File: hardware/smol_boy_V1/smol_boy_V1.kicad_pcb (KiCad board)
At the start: 2 copper layers, 21 parts, among them J1 Conn_01x01_Male, J2 Conn_01x06_Male, J3 Conn_01x04_Male, J4 Conn_01x03_Male, J5 Conn_01x03_Male, J6 Conn_01x03_Male, J7 Conn_01x03_Male, J8 Conn_01x03_Male, J9 Conn_01x03_Male, U1 ESP-12E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

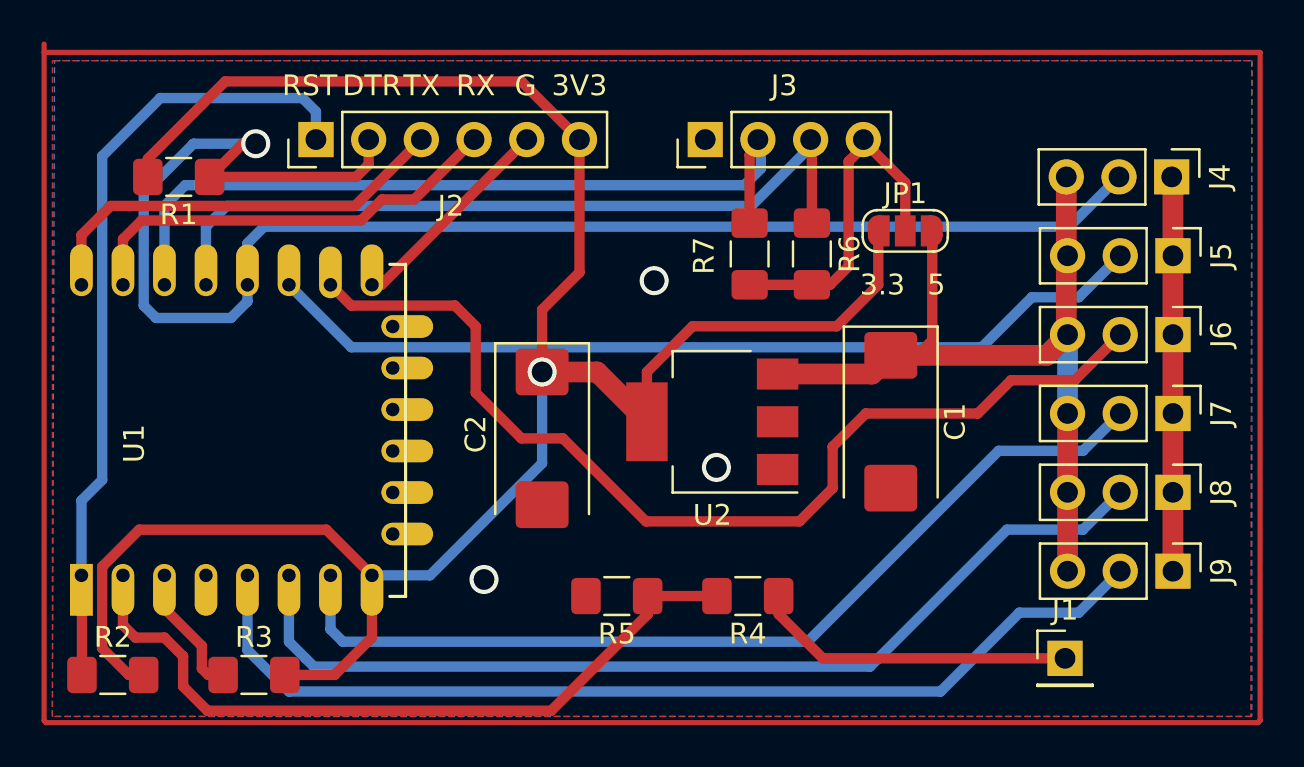
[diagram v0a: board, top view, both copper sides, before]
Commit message: fixed pcb channel pins
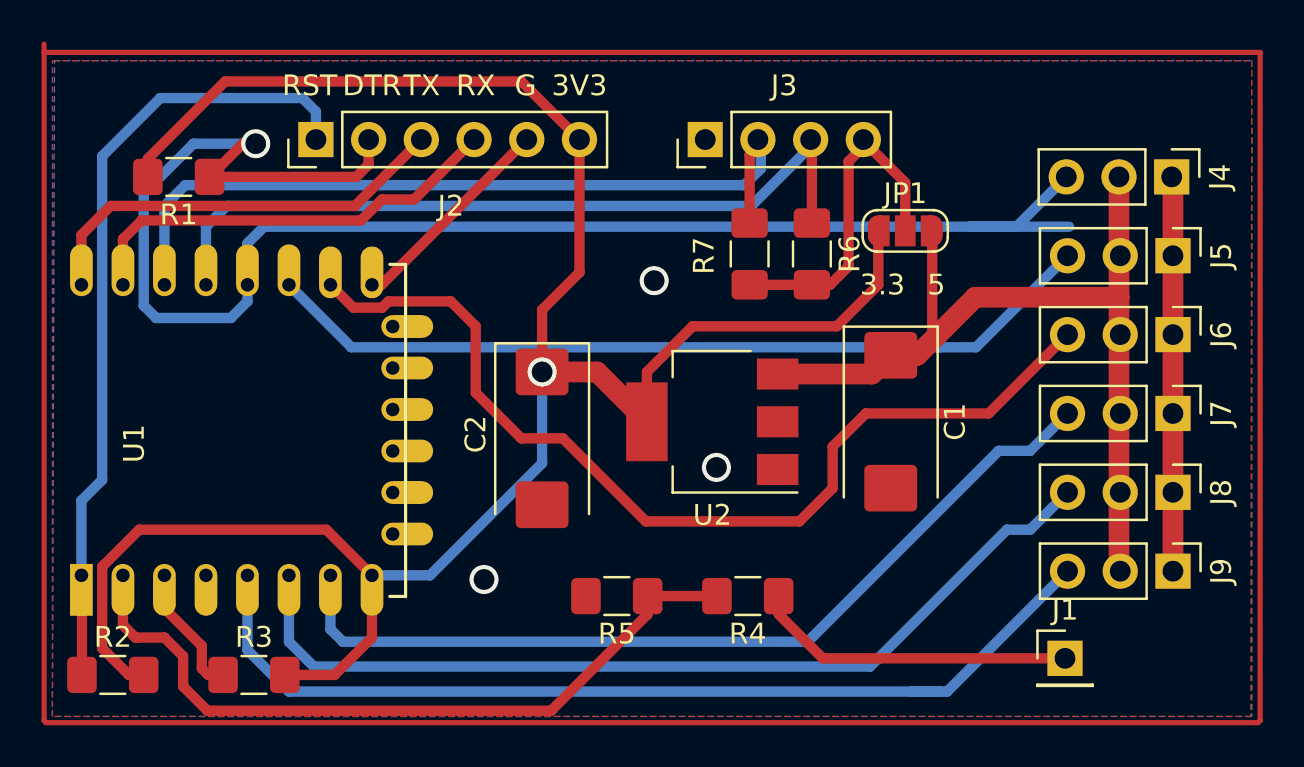
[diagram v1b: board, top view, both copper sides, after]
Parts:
- R5: value 10k -> 3.3k
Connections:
- J4 pad 2: CH0 -> +5V
- J4 pad 3: +5V -> CH0
- J5 pad 2: CH1 -> +5V
- J5 pad 3: +5V -> CH1
- J6 pad 2: CH2 -> +5V
- J6 pad 3: +5V -> CH2
- J7 pad 2: CH3 -> +5V
- J7 pad 3: +5V -> CH3
- J8 pad 2: CH4 -> +5V
- J8 pad 3: +5V -> CH4
- J9 pad 2: CH5 -> +5V
- J9 pad 3: +5V -> CH5
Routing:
- net CH1: track 43.1 -> 40.6 mm
- net CH3: track 45.5 -> 42.9 mm
- net CH4: track 47.2 -> 44.7 mm
- net CH0: track 75.5 -> 77.8 mm
- net CH2: track 49.6 -> 47.3 mm
- net +5V: track 41.4 -> 43.3 mm
- net CH5: track 48.9 -> 47.8 mm
